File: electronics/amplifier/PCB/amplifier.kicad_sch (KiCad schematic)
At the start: 22 parts, among them IC1 PA441DF, J1 Screw_Terminal_01x02, J2 Screw_Terminal_01x02, J3 Screw_Terminal_01x02, J4 Screw_Terminal_01x02, J5 BNC

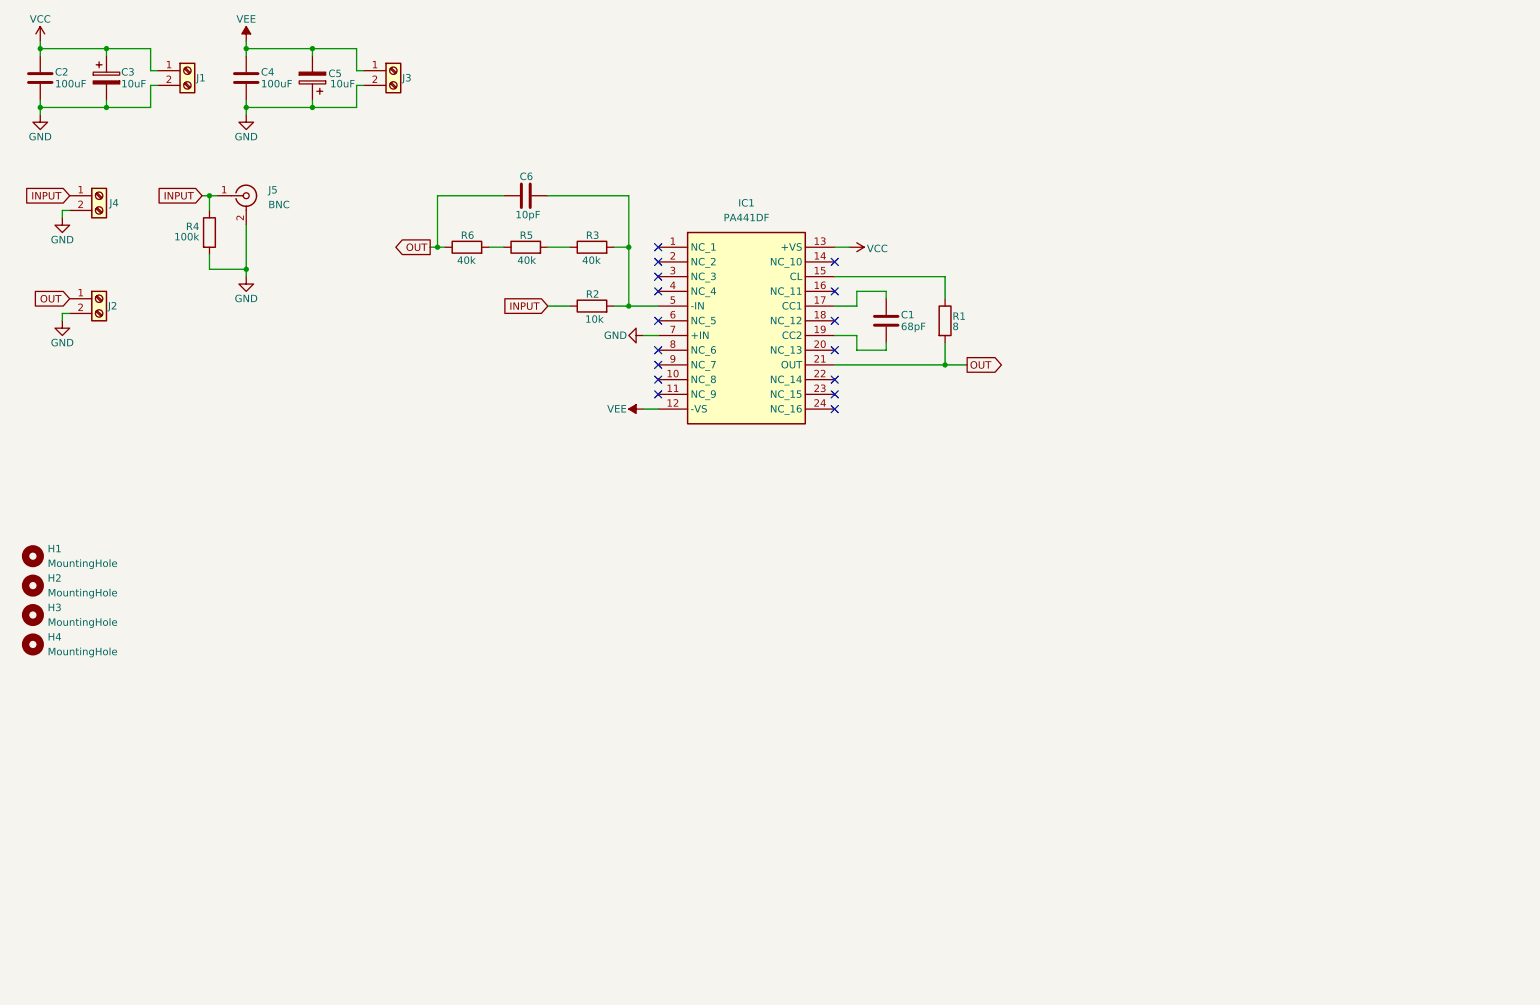
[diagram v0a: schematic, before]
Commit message: feat: amplifier board rev. 03
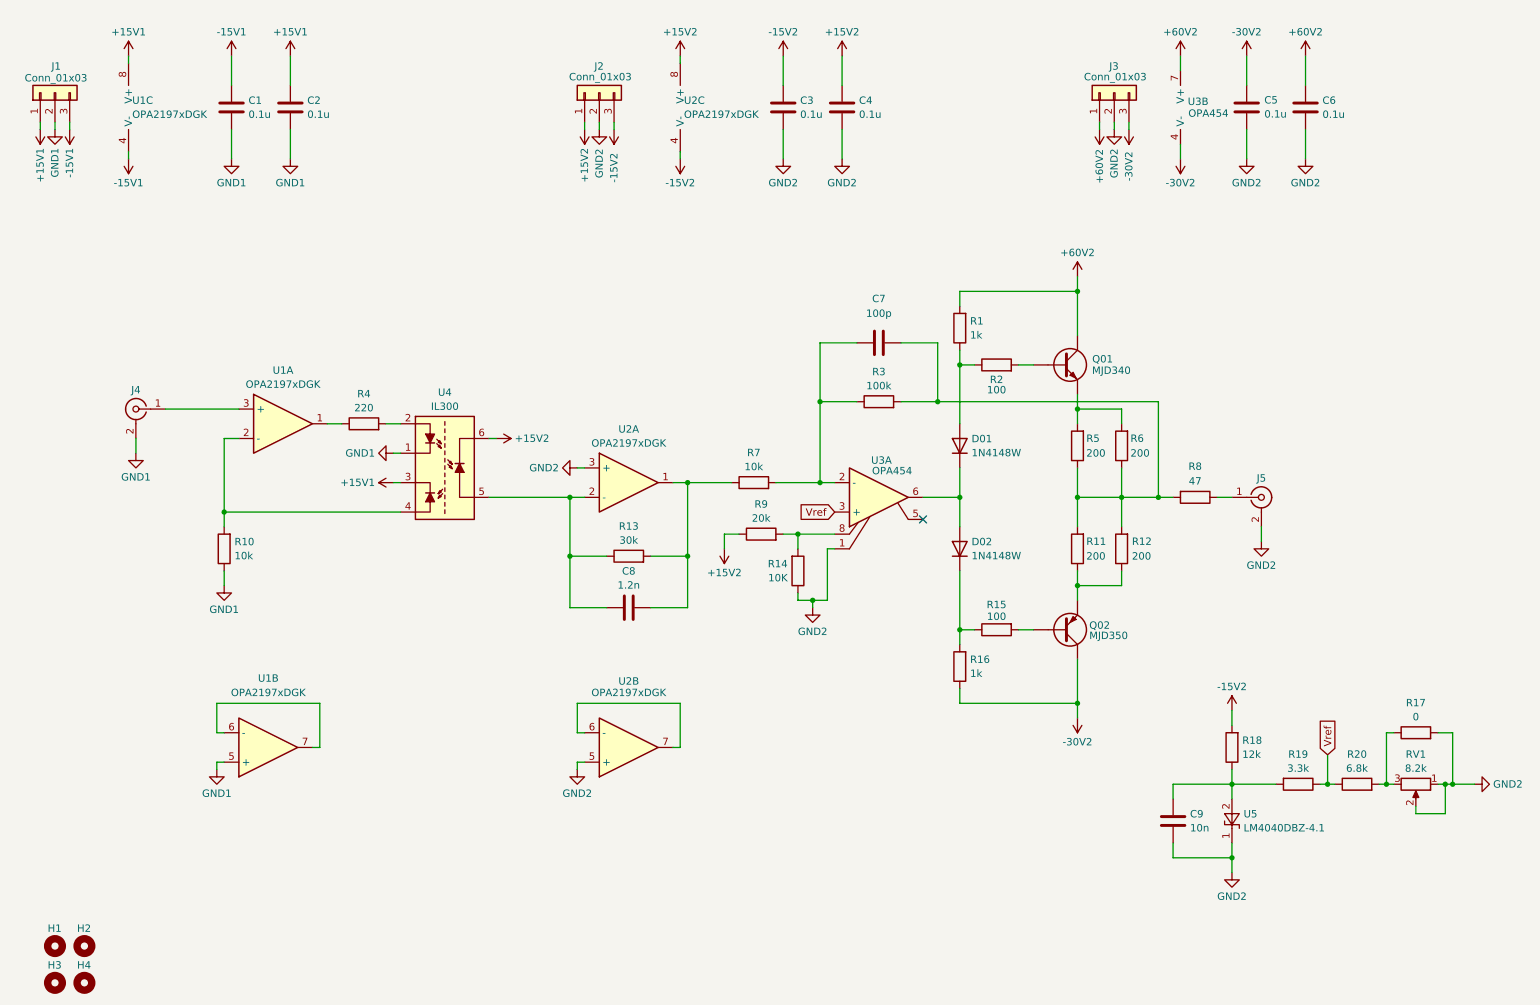
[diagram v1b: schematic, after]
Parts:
- removed C3, C5: 10uF, symbol Device:C_Polarized
- removed IC1: PA441DF, PA441DF, symbol PA441:PA441DF
- removed J1, J2, J3, J4: Screw_Terminal_01x02, MOLEX_CON:395011002_MOL, symbol Connector:Screw_Terminal_01x02
- added C3, C5: 0.1u, Resistor_SMD:R_0603_1608Metric, symbol Device:C
- added C7: 100p, Capacitor_SMD:C_0603_1608Metric, symbol Device:C
- added C8: 1.2n, Capacitor_SMD:C_0603_1608Metric, symbol Device:C
- added C9: 10n, Capacitor_SMD:C_0603_1608Metric, symbol Device:C
- added J1, J2, J3: Conn_01x03, TerminalBlock_Phoenix:TerminalBlock_Phoenix_PT-1,5-3-5.0-H_1x03_P5.00mm_Horizontal, symbol Connector_Generic:Conn_01x03
- added J4: Conn_Coaxial, Connector_Coaxial:SMA_Amphenol_132134_Vertical, symbol Connector:Conn_Coaxial
- added R10, R7: 10k, Resistor_SMD:R_0603_1608Metric, symbol Device:R
- added R11, R12: 200, Resistor_SMD:R_2512_6332Metric, symbol Device:R
- added R13: 30k, Resistor_SMD:R_0603_1608Metric, symbol Device:R
- added R14: 10K, Resistor_SMD:R_0603_1608Metric, symbol Device:R
- added R15: 100, Resistor_SMD:R_0603_1608Metric, symbol Device:R
- added R16: 1k, Resistor_SMD:R_0603_1608Metric, symbol Device:R
- added R17: 0, Resistor_SMD:R_0603_1608Metric, symbol Device:R
- added R18: 12k, Resistor_SMD:R_0603_1608Metric, symbol Device:R
- added R19: 3.3k, Resistor_SMD:R_0603_1608Metric, symbol Device:R
- added R20: 6.8k, Resistor_SMD:R_0603_1608Metric, symbol Device:R
- added R8: 47, Resistor_SMD:R_2512_6332Metric, symbol Device:R
- added R9: 20k, Resistor_SMD:R_0603_1608Metric, symbol Device:R
- added RV1: 8.2k, Potentiometer_THT:Potentiometer_Vishay_T93YA_Vertical, symbol Device:R_Potentiometer
- added U1, U2: OPA2197xDGK, Package_SO:VSSOP-8_3x3mm_P0.65mm, symbol Amplifier_Operational:OPA2197xDGK
- added U3: OPA454, amplifier:DDA0008J, symbol amplifier:OPA454
- added U4: IL300, Package_DIP:SMDIP-8_W9.53mm_Clearance8mm, symbol Isolator_Analog:IL300
- added U5: LM4040DBZ-4.1, Package_TO_SOT_SMD:SOT-23, symbol Reference_Voltage:LM4040DBZ-4.1
- C1: value 68pF -> 0.1u; footprint (none) -> Resistor_SMD:R_0603_1608Metric; Digikey (none) -> 399-C0603C104K5RACTUCT-ND
- C2, C4: value 100uF -> 0.1u; footprint (none) -> Resistor_SMD:R_0603_1608Metric; Digikey (none) -> 399-C0603C104K5RACTUCT-ND
- C6: value 10pF -> 0.1u; footprint (none) -> Resistor_SMD:R_0603_1608Metric; Digikey (none) -> 490-3285-1-ND
- J5: value BNC -> Conn_Coaxial; footprint (none) -> Connector_Coaxial:SMA_Amphenol_132134_Vertical; Digikey (none) -> 2073-RFPC-SMA28-F-ND
- R1: value 8 -> 1k; footprint (none) -> Resistor_SMD:R_0603_1608Metric; Digikey (none) -> 541-2788-1-ND
- R2: value 10k -> 100; footprint (none) -> Resistor_SMD:R_0603_1608Metric; Digikey (none) -> 541-2786-1-ND
- R3: value 40k -> 100k; footprint (none) -> Resistor_SMD:R_0805_2012Metric; Digikey (none) -> 541-2850-1-ND
- R4: value 100k -> 220; footprint (none) -> Resistor_SMD:R_0603_1608Metric; Digikey (none) -> 541-10437-1-ND
- R5, R6: value 40k -> 200; footprint (none) -> Resistor_SMD:R_2512_6332Metric; Digikey (none) -> A116015CT-ND
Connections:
- net -15V1: now reaches C1.1
- net -15V1: now also J1.3 (Pin_3), U1.4 (V-)
- net GND1: now reaches C1.2
- net GND1: now also C2.2, J1.2 (Pin_2), J4.2 (Ext), R10.1, U1.5 (+), U4.1
- net at R1.1: now also R2.1
- net at R3.1: now also C7.1, R7.2, U3.2 (-); no longer R5.2
- net at R5.1: now also R3.2, R6.1, C7.2, R11.2, R12.2, R8.2; no longer R6.2
- net GND renamed GND2
- net GND2: now also C6.2, C3.2, C5.2, C9.1, J2.2 (Pin_2), J3.2 (Pin_2), R14.1, R17.2, RV1.1, RV1.2, U2.3 (+), U2.5 (+), U3.1, U5.1 (K); no longer C2.2, R4.2
- removed net INPUT: J5.1 (In), R2.1, R4.1
- net OUT renamed +60V2
- net +60V2: now also J3.1 (Pin_1), U3.7 (V+); no longer R6.1
- net VCC renamed +15V1
- net +15V1: now also J1.1 (Pin_1), U1.8 (V+), U4.3
- net VEE renamed +15V2
- net +15V2: now also J2.1 (Pin_1), R9.1, U2.8 (V+), U4.6
- new net: C9.2, R18.1, R19.2, U5.2 (A)
- new net: R14.2, R9.2, U3.8
- new net: J5.1 (In), R8.1
- new net: J4.1 (In), U1.3 (+)
- new net: R17.1, R20.2, RV1.3
- new net: R11.1, R12.1
- new net: C8.2, R13.2, R7.1, U2.1
- new net: U2.6 (-), U2.7
- new net: R15.1, R16.2
- new net: R5.2, R6.2
- new net: C8.1, R13.1, U2.2 (-), U4.5
- new net: R4.2, U4.2
- new net: R10.2, U1.2 (-), U4.4
- new net: R4.1, U1.1
- new net: U1.6 (-), U1.7
- new net -15V2: C3.1, J2.3 (Pin_3), R18.2, U2.4 (V-)
- new net -30V2: C5.1, J3.3 (Pin_3), R16.1, U3.4 (V-)
- new net Vref: R19.1, R20.1, U3.3 (+)
- now unconnected: R2.2
- no-connect marks 16 -> 1
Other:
- title: (none) -> Nanopositioner
